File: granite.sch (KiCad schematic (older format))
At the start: 15 parts, among them IC1 ATMEGA32U4, SW1 SW_PUSH, Y1 16MHz

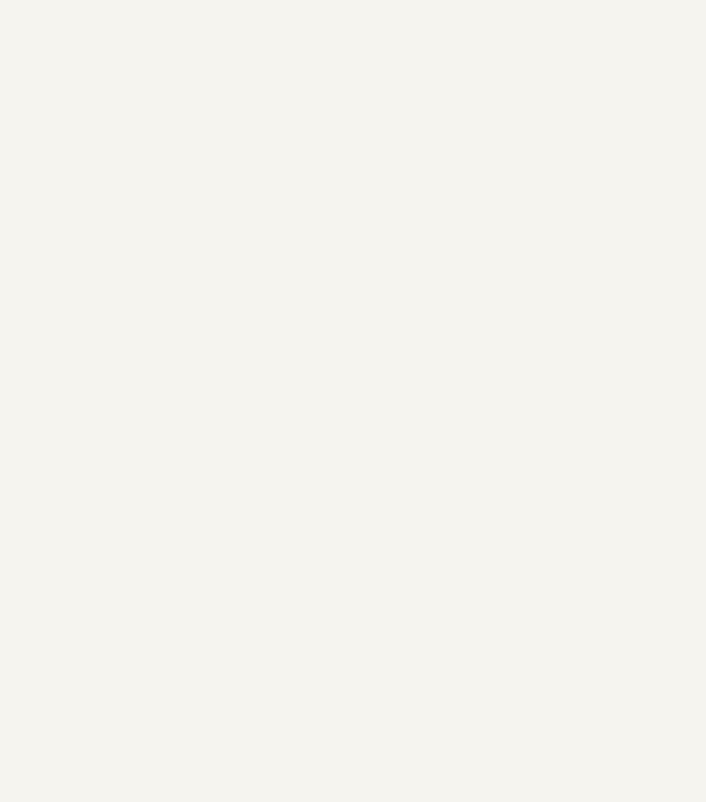
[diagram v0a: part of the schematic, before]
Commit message: usb footprint
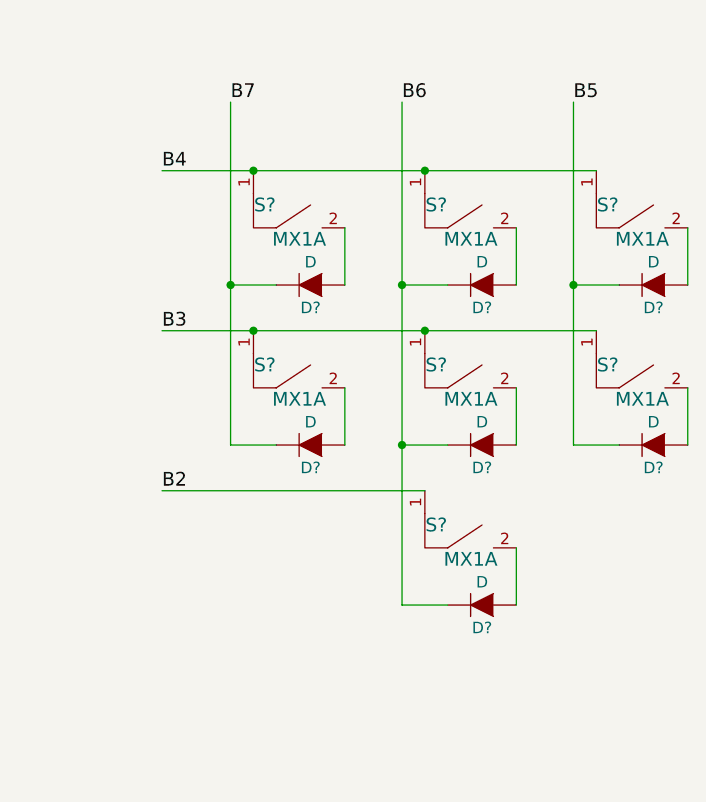
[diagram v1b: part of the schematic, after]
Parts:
- added D? (x7): D, symbol D
- added S? (x7): MX1A, symbol MX1A
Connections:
- net B2: now also S?.1
- net B3: now also S?.1, S?.1, S?.1
- net B4: now also S?.1, S?.1, S?.1
- net B5: now also D?.2 (K), D?.2 (K)
- net B6: now also D?.2 (K), D?.2 (K), D?.2 (K)
- net B7: now also D?.2 (K), D?.2 (K)
- new net: D?.1 (A), S?.2 (x7)
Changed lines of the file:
@@
 LIBS:atmega
 LIBS:mx1a
-LIBS:usb-b
 LIBS:granite-cache
 EELAYER 25 0
@@
 	-1   0    0    1
 $EndComp
+$Comp
+L MX1A S?
+U 1 1 55BD7CBD
+P 11700 4200
+F 0 "S?" H 11550 4450 60  0000 C CNN
+F 1 "MX1A" H 11700 4300 60  0000 C CNN
+F 2 "" H 11700 4200 60  0000 C CNN
+F 3 "" H 11700 4200 60  0000 C CNN
+	1    11700 4200
+	1    0    0    -1
+$EndComp
+$Comp
+L D D?
+U 1 1 55BD8384
+P 11750 4300
+F 0 "D?" H 11750 4400 50  0000 C CNN
+F 1 "D" H 11750 4200 50  0000 C CNN
+F 2 "" H 11750 4300 60  0000 C CNN
+F 3 "" H 11750 4300 60  0000 C CNN
+	1    11750 4300
+	-1   0    0    1
+$EndComp
+Wire Wire Line
+	11900 4050 11900 4300
+Wire Wire Line
+	11600 4300 11400 4300
+$Comp
+L MX1A S?
+U 1 1 55BD8711
+P 12450 4200
+F 0 "S?" H 12300 4450 60  0000 C CNN
+F 1 "MX1A" H 12450 4300 60  0000 C CNN
+F 2 "" H 12450 4200 60  0000 C CNN
+F 3 "" H 12450 4200 60  0000 C CNN
+	1    12450 4200
+	1    0    0    -1
+$EndComp
+$Comp
+L D D?
+U 1 1 55BD8717
+P 12500 4300
+F 0 "D?" H 12500 4400 50  0000 C CNN
+F 1 "D" H 12500 4200 50  0000 C CNN
+F 2 "" H 12500 4300 60  0000 C CNN
+F 3 "" H 12500 4300 60  0000 C CNN
+	1    12500 4300
+	-1   0    0    1
+$EndComp
+Wire Wire Line
+	12650 4050 12650 4300
+Wire Wire Line
+	12350 4300 12150 4300
+$Comp
+L MX1A S?
+U 1 1 55BD8B24
+P 13200 4200
+F 0 "S?" H 13050 4450 60  0000 C CNN
+F 1 "MX1A" H 13200 4300 60  0000 C CNN
+F 2 "" H 13200 4200 60  0000 C CNN
+F 3 "" H 13200 4200 60  0000 C CNN
+	1    13200 4200
+	1    0    0    -1
+$EndComp
+$Comp
+L D D?
+U 1 1 55BD8B2A
+P 13250 4300
+F 0 "D?" H 13250 4400 50  0000 C CNN
+F 1 "D" H 13250 4200 50  0000 C CNN
+F 2 "" H 13250 4300 60  0000 C CNN
+F 3 "" H 13250 4300 60  0000 C CNN
+	1    13250 4300
+	-1   0    0    1
+$EndComp
+Wire Wire Line
+	13400 4050 13400 4300
+Wire Wire Line
+	13100 4300 12900 4300
+$Comp
+L MX1A S?
+U 1 1 55BD8CBB
+P 11700 4900
+F 0 "S?" H 11550 5150 60  0000 C CNN
+F 1 "MX1A" H 11700 5000 60  0000 C CNN
+F 2 "" H 11700 4900 60  0000 C CNN
+F 3 "" H 11700 4900 60  0000 C CNN
+	1    11700 4900
+	1    0    0    -1
+$EndComp
+$Comp
+L D D?
+U 1 1 55BD8CC1
+P 11750 5000
+F 0 "D?" H 11750 5100 50  0000 C CNN
+F 1 "D" H 11750 4900 50  0000 C CNN
+F 2 "" H 11750 5000 60  0000 C CNN
+F 3 "" H 11750 5000 60  0000 C CNN
+	1    11750 5000
+	-1   0    0    1
+$EndComp
+Wire Wire Line
+	11900 4750 11900 5000
+Wire Wire Line
+	11600 5000 11400 5000
+$Comp
+L MX1A S?
+U 1 1 55BD8CC9
+P 12450 4900
+F 0 "S?" H 12300 5150 60  0000 C CNN
+F 1 "MX1A" H 12450 5000 60  0000 C CNN
+F 2 "" H 12450 4900 60  0000 C CNN
+F 3 "" H 12450 4900 60  0000 C CNN
+	1    12450 4900
+	1    0    0    -1
+$EndComp
+$Comp
+L D D?
+U 1 1 55BD8CCF
+P 12500 5000
+F 0 "D?" H 12500 5100 50  0000 C CNN
+F 1 "D" H 12500 4900 50  0000 C CNN
+F 2 "" H 12500 5000 60  0000 C CNN
+F 3 "" H 12500 5000 60  0000 C CNN
+	1    12500 5000
+	-1   0    0    1
+$EndComp
+Wire Wire Line
+	12650 4750 12650 5000
+Wire Wire Line
+	12350 5000 12150 5000
+$Comp
+L MX1A S?
+U 1 1 55BD8CD7
+P 13200 4900
+F 0 "S?" H 13050 5150 60  0000 C CNN
+F 1 "MX1A" H 13200 5000 60  0000 C CNN
+F 2 "" H 13200 4900 60  0000 C CNN
+F 3 "" H 13200 4900 60  0000 C CNN
+	1    13200 4900
+	1    0    0    -1
+$EndComp
+$Comp
+L D D?
+U 1 1 55BD8CDD
+P 13250 5000
+F 0 "D?" H 13250 5100 50  0000 C CNN
+F 1 "D" H 13250 4900 50  0000 C CNN
+F 2 "" H 13250 5000 60  0000 C CNN
+F 3 "" H 13250 5000 60  0000 C CNN
+	1    13250 5000
+	-1   0    0    1
+$EndComp
+Wire Wire Line
+	13400 4750 13400 5000
+Wire Wire Line
+	13100 5000 12900 5000
+$Comp
+L MX1A S?
+U 1 1 55BD8D79
+P 12450 5600
+F 0 "S?" H 12300 5850 60  0000 C CNN
+F 1 "MX1A" H 12450 5700 60  0000 C CNN
+F 2 "" H 12450 5600 60  0000 C CNN
+F 3 "" H 12450 5600 60  0000 C CNN
+	1    12450 5600
+	1    0    0    -1
+$EndComp
+$Comp
+L D D?
+U 1 1 55BD8D7F
+P 12500 5700
+F 0 "D?" H 12500 5800 50  0000 C CNN
+F 1 "D" H 12500 5600 50  0000 C CNN
+F 2 "" H 12500 5700 60  0000 C CNN
+F 3 "" H 12500 5700 60  0000 C CNN
+	1    12500 5700
+	-1   0    0    1
+$EndComp
+Wire Wire Line
+	12650 5450 12650 5700
+Wire Wire Line
+	12350 5700 12150 5700
+Wire Wire Line
+	11100 3800 13000 3800
+Connection ~ 12250 3800
+Connection ~ 11500 3800
+Wire Wire Line
+	11100 4500 13000 4500
+Connection ~ 12250 4500
+Connection ~ 11500 4500
+Wire Wire Line
+	11100 5200 12250 5200
+Wire Wire Line
+	11400 5000 11400 3500
+Connection ~ 11400 4300
+Wire Wire Line
+	12150 5700 12150 3500
+Connection ~ 12150 5000
+Connection ~ 12150 4300
+Wire Wire Line
+	12900 5000 12900 3500
+Connection ~ 12900 4300
+Text Label 11400 3500 0    60   ~ 0
+B7
+Text Label 12150 3500 0    60   ~ 0
+B6
+Text Label 12900 3500 0    60   ~ 0
+B5
+Text Label 11100 3800 0    60   ~ 0
+B4
+Text Label 11100 4500 0    60   ~ 0
+B3
+Text Label 11100 5200 0    60   ~ 0
+B2
 $EndSCHEMATC

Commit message: annotations in schematic
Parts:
- gave numbers to parts that had none: 15
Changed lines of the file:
@@
 F0
 $Comp
-L USB-MINI-B CON?
+L USB-MINI-B CON1
 U 1 1 55B72E69
 P 1850 6250
-F 0 "CON?" H 2100 6600 50  0000 C CNN
+F 0 "CON1" H 2100 6600 50  0000 C CNN
 F 1 "USB-MINI-B WM17115-ND" H 2000 5900 50  0000 C CNN
 F 2 "" H 1850 6150 50  0000 C CNN
@@
 	1100 6200 1100 6350
 $Comp
-L GNDREF #PWR?
+L GNDREF #PWR010
 U 1 1 55B87288
 P 1100 6350
-F 0 "#PWR?" H 1100 6100 60  0001 C CNN
+F 0 "#PWR010" H 1100 6100 60  0001 C CNN
 F 1 "GNDREF" H 1100 6200 60  0000 C CNN
 F 2 "" H 1100 6350 60  0000 C CNN
@@
 	3050 7000 3050 7450
 $Comp
-L GNDREF #PWR?
+L GNDREF #PWR011
 U 1 1 55B88521
 P 3050 7450
-F 0 "#PWR?" H 3050 7200 60  0001 C CNN
+F 0 "#PWR011" H 3050 7200 60  0001 C CNN
 F 1 "GNDREF" H 3050 7300 60  0000 C CNN
 F 2 "" H 3050 7450 60  0000 C CNN
@@
 	1100 5500 3450 5500
 $Comp
-L GNDREF #PWR?
+L GNDREF #PWR012
 U 1 1 55BC6395
 P 1600 6650
-F 0 "#PWR?" H 1600 6400 60  0001 C CNN
+F 0 "#PWR012" H 1600 6400 60  0001 C CNN
 F 1 "GNDREF" H 1600 6500 60  0000 C CNN
 F 2 "" H 1600 6650 60  0000 C CNN
@@
 $EndComp
 $Comp
-L GNDREF #PWR?
+L GNDREF #PWR013
 U 1 1 55BC6520
 P 1600 5850
-F 0 "#PWR?" H 1600 5600 60  0001 C CNN
+F 0 "#PWR013" H 1600 5600 60  0001 C CNN
 F 1 "GNDREF" H 1600 5700 60  0000 C CNN
 F 2 "" H 1600 5850 60  0000 C CNN
@@
 $EndComp
 $Comp
-L MX1A S?
+L MX1A S1
 U 1 1 55BD7CBD
 P 11700 4200
-F 0 "S?" H 11550 4450 60  0000 C CNN
+F 0 "S1" H 11550 4450 60  0000 C CNN
 F 1 "MX1A" H 11700 4300 60  0000 C CNN
 F 2 "" H 11700 4200 60  0000 C CNN
@@
 $EndComp
 $Comp
-L D D?
+L D D1
 U 1 1 55BD8384
 P 11750 4300
-F 0 "D?" H 11750 4400 50  0000 C CNN
+F 0 "D1" H 11750 4400 50  0000 C CNN
 F 1 "D" H 11750 4200 50  0000 C CNN
 F 2 "" H 11750 4300 60  0000 C CNN
@@
 	11600 4300 11400 4300
 $Comp
-L MX1A S?
+L MX1A S3
 U 1 1 55BD8711
 P 12450 4200
-F 0 "S?" H 12300 4450 60  0000 C CNN
+F 0 "S3" H 12300 4450 60  0000 C CNN
 F 1 "MX1A" H 12450 4300 60  0000 C CNN
 F 2 "" H 12450 4200 60  0000 C CNN
@@
 $EndComp
 $Comp
-L D D?
+L D D3
 U 1 1 55BD8717
 P 12500 4300
-F 0 "D?" H 12500 4400 50  0000 C CNN
+F 0 "D3" H 12500 4400 50  0000 C CNN
 F 1 "D" H 12500 4200 50  0000 C CNN
 F 2 "" H 12500 4300 60  0000 C CNN
@@
 	12350 4300 12150 4300
 $Comp
-L MX1A S?
+L MX1A S6
 U 1 1 55BD8B24
 P 13200 4200
-F 0 "S?" H 13050 4450 60  0000 C CNN
+F 0 "S6" H 13050 4450 60  0000 C CNN
 F 1 "MX1A" H 13200 4300 60  0000 C CNN
 F 2 "" H 13200 4200 60  0000 C CNN
@@
 $EndComp
 $Comp
-L D D?
+L D D6
 U 1 1 55BD8B2A
 P 13250 4300
-F 0 "D?" H 13250 4400 50  0000 C CNN
+F 0 "D6" H 13250 4400 50  0000 C CNN
 F 1 "D" H 13250 4200 50  0000 C CNN
 F 2 "" H 13250 4300 60  0000 C CNN
@@
 	13100 4300 12900 4300
 $Comp
-L MX1A S?
+L MX1A S2
 U 1 1 55BD8CBB
 P 11700 4900
-F 0 "S?" H 11550 5150 60  0000 C CNN
+F 0 "S2" H 11550 5150 60  0000 C CNN
 F 1 "MX1A" H 11700 5000 60  0000 C CNN
 F 2 "" H 11700 4900 60  0000 C CNN
@@
 $EndComp
 $Comp
-L D D?
+L D D2
 U 1 1 55BD8CC1
 P 11750 5000
-F 0 "D?" H 11750 5100 50  0000 C CNN
+F 0 "D2" H 11750 5100 50  0000 C CNN
 F 1 "D" H 11750 4900 50  0000 C CNN
 F 2 "" H 11750 5000 60  0000 C CNN
@@
 	11600 5000 11400 5000
 $Comp
-L MX1A S?
+L MX1A S4
 U 1 1 55BD8CC9
 P 12450 4900
-F 0 "S?" H 12300 5150 60  0000 C CNN
+F 0 "S4" H 12300 5150 60  0000 C CNN
 F 1 "MX1A" H 12450 5000 60  0000 C CNN
 F 2 "" H 12450 4900 60  0000 C CNN
@@
 $EndComp
 $Comp
-L D D?
+L D D4
 U 1 1 55BD8CCF
 P 12500 5000
-F 0 "D?" H 12500 5100 50  0000 C CNN
+F 0 "D4" H 12500 5100 50  0000 C CNN
 F 1 "D" H 12500 4900 50  0000 C CNN
 F 2 "" H 12500 5000 60  0000 C CNN
@@
 	12350 5000 12150 5000
 $Comp
-L MX1A S?
+L MX1A S7
 U 1 1 55BD8CD7
 P 13200 4900
-F 0 "S?" H 13050 5150 60  0000 C CNN
+F 0 "S7" H 13050 5150 60  0000 C CNN
 F 1 "MX1A" H 13200 5000 60  0000 C CNN
 F 2 "" H 13200 4900 60  0000 C CNN
@@
 $EndComp
 $Comp
-L D D?
+L D D7
 U 1 1 55BD8CDD
 P 13250 5000
-F 0 "D?" H 13250 5100 50  0000 C CNN
+F 0 "D7" H 13250 5100 50  0000 C CNN
 F 1 "D" H 13250 4900 50  0000 C CNN
 F 2 "" H 13250 5000 60  0000 C CNN
@@
 	13100 5000 12900 5000
 $Comp
-L MX1A S?
+L MX1A S5
 U 1 1 55BD8D79
 P 12450 5600
-F 0 "S?" H 12300 5850 60  0000 C CNN
+F 0 "S5" H 12300 5850 60  0000 C CNN
 F 1 "MX1A" H 12450 5700 60  0000 C CNN
 F 2 "" H 12450 5600 60  0000 C CNN
@@
 $EndComp
 $Comp
-L D D?
+L D D5
 U 1 1 55BD8D7F
 P 12500 5700
-F 0 "D?" H 12500 5800 50  0000 C CNN
+F 0 "D5" H 12500 5800 50  0000 C CNN
 F 1 "D" H 12500 5600 50  0000 C CNN
 F 2 "" H 12500 5700 60  0000 C CNN

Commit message: mx1a footprints
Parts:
- C1, C2, C3: value 0.1uF -> 100nF; footprint Capacitors_SMD:C_0603_HandSoldering -> Capacitors_SMD:C_0805_HandSoldering
- C4, C5, C6: footprint Capacitors_SMD:C_0603_HandSoldering -> Capacitors_SMD:C_0805_HandSoldering
- C7: value 0.1uF -> 100nF; footprint (none) -> Capacitors_SMD:C_0805_HandSoldering
- C8: footprint (none) -> Capacitors_SMD:C_0805_HandSoldering
- CON1: footprint (none) -> bwu-keyboard:USB-MINI-B-WM17115-ND
- D0:0: renamed from D1; footprint (none) -> SM0805:SOD-123
- D0:1: renamed from D3; footprint (none) -> SM0805:SOD-123
- D0:2: renamed from D6; footprint (none) -> SM0805:SOD-123
- D1:0: renamed from D2; footprint (none) -> SM0805:SOD-123
- D1:1: renamed from D4; footprint (none) -> SM0805:SOD-123
- D1:2: renamed from D7; footprint (none) -> SM0805:SOD-123
- D2:1: renamed from D5; footprint (none) -> SM0805:SOD-123
- R1, R2, R3: footprint Resistors_SMD:R_0603_HandSoldering -> Resistors_SMD:R_0805_HandSoldering
- S0:0: renamed from S1; footprint (none) -> CHERRY_PCB_100H:CHERRY_PCB_100H
- S0:1: renamed from S3; footprint (none) -> CHERRY_PCB_100H:CHERRY_PCB_100H
- S0:2: renamed from S6; footprint (none) -> CHERRY_PCB_100H:CHERRY_PCB_100H
- S1:0: renamed from S2; footprint (none) -> CHERRY_PCB_100H:CHERRY_PCB_100H
- S1:1: renamed from S4; footprint (none) -> CHERRY_PCB_100H:CHERRY_PCB_100H
- S1:2: renamed from S7; footprint (none) -> CHERRY_PCB_100H:CHERRY_PCB_100H
- S2:1: renamed from S5; footprint (none) -> CHERRY_PCB_100H:CHERRY_PCB_100H
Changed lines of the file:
@@
 LIBS:atmega
 LIBS:mx1a
+LIBS:usb-b
 LIBS:granite-cache
 EELAYER 25 0
@@
 F 0 "C6" H 2775 6950 50  0000 L CNN
 F 1 "1uF" H 2775 6750 50  0000 L CNN
-F 2 "Capacitors_SMD:C_0603_HandSoldering" H 2750 6850 60  0001 C CNN
+F 2 "Capacitors_SMD:C_0805_HandSoldering" H 2750 6850 60  0001 C CNN
 F 3 "" H 2750 6850 60  0000 C CNN
 	1    2750 6850
@@
 P 3000 3400
 F 0 "C3" H 3025 3500 50  0000 L CNN
-F 1 "0.1uF" H 3025 3300 50  0000 L CNN
-F 2 "Capacitors_SMD:C_0603_HandSoldering" H 3000 3400 60  0001 C CNN
+F 1 "100nF" H 3025 3300 50  0000 L CNN
+F 2 "Capacitors_SMD:C_0805_HandSoldering" H 3000 3400 60  0001 C CNN
 F 3 "" H 3000 3400 60  0000 C CNN
 	1    3000 3400
@@
 P 2700 3400
 F 0 "C2" H 2725 3500 50  0000 L CNN
-F 1 "0.1uF" H 2725 3300 50  0000 L CNN
-F 2 "Capacitors_SMD:C_0603_HandSoldering" H 2700 3400 60  0001 C CNN
+F 1 "100nF" H 2725 3300 50  0000 L CNN
+F 2 "Capacitors_SMD:C_0805_HandSoldering" H 2700 3400 60  0001 C CNN
 F 3 "" H 2700 3400 60  0000 C CNN
 	1    2700 3400
@@
 P 2400 3400
 F 0 "C1" H 2425 3500 50  0000 L CNN
-F 1 "0.1uF" H 2425 3300 50  0000 L CNN
-F 2 "Capacitors_SMD:C_0603_HandSoldering" H 2400 3400 60  0001 C CNN
+F 1 "100nF" H 2425 3300 50  0000 L CNN
+F 2 "Capacitors_SMD:C_0805_HandSoldering" H 2400 3400 60  0001 C CNN
 F 3 "" H 2400 3400 60  0000 C CNN
 	1    2400 3400
@@
 F 0 "R2" V 3030 6300 50  0000 C CNN
 F 1 "22" V 2950 6300 50  0000 C CNN
-F 2 "Resistors_SMD:R_0603_HandSoldering" V 2880 6300 30  0001 C CNN
+F 2 "Resistors_SMD:R_0805_HandSoldering" V 2880 6300 30  0001 C CNN
 F 3 "" H 2950 6300 30  0000 C CNN
 	1    2950 6300
@@
 F 0 "R1" V 3030 6100 50  0000 C CNN
 F 1 "22" V 2950 6100 50  0000 C CNN
-F 2 "Resistors_SMD:R_0603_HandSoldering" V 2880 6100 30  0001 C CNN
+F 2 "Resistors_SMD:R_0805_HandSoldering" V 2880 6100 30  0001 C CNN
 F 3 "" H 2950 6100 30  0000 C CNN
 	1    2950 6100
@@
 F 0 "C4" H 2125 5000 50  0000 L CNN
 F 1 "10pF" H 2125 4800 50  0000 L CNN
-F 2 "Capacitors_SMD:C_0603_HandSoldering" H 2100 4900 60  0001 C CNN
+F 2 "Capacitors_SMD:C_0805_HandSoldering" H 2100 4900 60  0001 C CNN
 F 3 "" H 2100 4900 60  0000 C CNN
 	1    2100 4900
@@
 F 0 "C5" H 2725 5000 50  0000 L CNN
 F 1 "10pF" H 2725 4800 50  0000 L CNN
-F 2 "Capacitors_SMD:C_0603_HandSoldering" H 2700 4900 60  0001 C CNN
+F 2 "Capacitors_SMD:C_0805_HandSoldering" H 2700 4900 60  0001 C CNN
 F 3 "" H 2700 4900 60  0000 C CNN
 	1    2700 4900
@@
 F 0 "R3" V 5280 7400 50  0000 C CNN
 F 1 "1K" V 5200 7400 50  0000 C CNN
-F 2 "Resistors_SMD:R_0603_HandSoldering" V 5130 7400 30  0001 C CNN
+F 2 "Resistors_SMD:R_0805_HandSoldering" V 5130 7400 30  0001 C CNN
 F 3 "" H 5200 7400 30  0000 C CNN
 	1    5200 7400
@@
 F 0 "CON1" H 2100 6600 50  0000 C CNN
 F 1 "USB-MINI-B WM17115-ND" H 2000 5900 50  0000 C CNN
-F 2 "" H 1850 6150 50  0000 C CNN
+F 2 "bwu-keyboard:USB-MINI-B-WM17115-ND" H 1850 6150 50  0001 C CNN
 F 3 "" H 1850 6150 50  0000 C CNN
 	1    1850 6250
@@
 P 1100 6050
 F 0 "C7" H 1125 6150 50  0000 L CNN
-F 1 "0.1uF" H 1125 5950 50  0000 L CNN
-F 2 "" H 1100 6050 60  0000 C CNN
+F 1 "100nF" H 1125 5950 50  0000 L CNN
+F 2 "Capacitors_SMD:C_0805_HandSoldering" H 1100 6050 60  0001 C CNN
 F 3 "" H 1100 6050 60  0000 C CNN
 	1    1100 6050
@@
 F 0 "C8" H 3075 6950 50  0000 L CNN
 F 1 "1uF" H 3075 6750 50  0000 L CNN
-F 2 "" H 3050 6850 60  0000 C CNN
+F 2 "Capacitors_SMD:C_0805_HandSoldering" H 3050 6850 60  0001 C CNN
 F 3 "" H 3050 6850 60  0000 C CNN
 	1    3050 6850
@@
 $EndComp
 $Comp
-L MX1A S1
+L MX1A S0:0
 U 1 1 55BD7CBD
 P 11700 4200
-F 0 "S1" H 11550 4450 60  0000 C CNN
+F 0 "S0:0" H 11550 4450 60  0000 C CNN
 F 1 "MX1A" H 11700 4300 60  0000 C CNN
-F 2 "" H 11700 4200 60  0000 C CNN
+F 2 "CHERRY_PCB_100H:CHERRY_PCB_100H" H 11700 4200 60  0001 C CNN
 F 3 "" H 11700 4200 60  0000 C CNN
 	1    11700 4200
@@
 $EndComp
 $Comp
-L D D1
+L D D0:0
 U 1 1 55BD8384
 P 11750 4300
-F 0 "D1" H 11750 4400 50  0000 C CNN
+F 0 "D0:0" H 11750 4400 50  0000 C CNN
 F 1 "D" H 11750 4200 50  0000 C CNN
-F 2 "" H 11750 4300 60  0000 C CNN
+F 2 "SM0805:SOD-123" H 11750 4300 60  0001 C CNN
 F 3 "" H 11750 4300 60  0000 C CNN
 	1    11750 4300
@@
 	11600 4300 11400 4300
 $Comp
-L MX1A S3
+L MX1A S0:1
 U 1 1 55BD8711
 P 12450 4200
-F 0 "S3" H 12300 4450 60  0000 C CNN
+F 0 "S0:1" H 12300 4450 60  0000 C CNN
 F 1 "MX1A" H 12450 4300 60  0000 C CNN
-F 2 "" H 12450 4200 60  0000 C CNN
+F 2 "CHERRY_PCB_100H:CHERRY_PCB_100H" H 12450 4200 60  0001 C CNN
 F 3 "" H 12450 4200 60  0000 C CNN
 	1    12450 4200
@@
 $EndComp
 $Comp
-L D D3
+L D D0:1
 U 1 1 55BD8717
 P 12500 4300
-F 0 "D3" H 12500 4400 50  0000 C CNN
+F 0 "D0:1" H 12500 4400 50  0000 C CNN
 F 1 "D" H 12500 4200 50  0000 C CNN
-F 2 "" H 12500 4300 60  0000 C CNN
+F 2 "SM0805:SOD-123" H 12500 4300 60  0001 C CNN
 F 3 "" H 12500 4300 60  0000 C CNN
 	1    12500 4300
@@
 	12350 4300 12150 4300
 $Comp
-L MX1A S6
+L MX1A S0:2
 U 1 1 55BD8B24
 P 13200 4200
-F 0 "S6" H 13050 4450 60  0000 C CNN
+F 0 "S0:2" H 13050 4450 60  0000 C CNN
 F 1 "MX1A" H 13200 4300 60  0000 C CNN
-F 2 "" H 13200 4200 60  0000 C CNN
+F 2 "CHERRY_PCB_100H:CHERRY_PCB_100H" H 13200 4200 60  0001 C CNN
 F 3 "" H 13200 4200 60  0000 C CNN
 	1    13200 4200
@@
 $EndComp
 $Comp
-L D D6
+L D D0:2
 U 1 1 55BD8B2A
 P 13250 4300
-F 0 "D6" H 13250 4400 50  0000 C CNN
+F 0 "D0:2" H 13250 4400 50  0000 C CNN
 F 1 "D" H 13250 4200 50  0000 C CNN
-F 2 "" H 13250 4300 60  0000 C CNN
+F 2 "SM0805:SOD-123" H 13250 4300 60  0001 C CNN
 F 3 "" H 13250 4300 60  0000 C CNN
 	1    13250 4300
@@
 	13100 4300 12900 4300
 $Comp
-L MX1A S2
+L MX1A S1:0
 U 1 1 55BD8CBB
 P 11700 4900
-F 0 "S2" H 11550 5150 60  0000 C CNN
+F 0 "S1:0" H 11550 5150 60  0000 C CNN
 F 1 "MX1A" H 11700 5000 60  0000 C CNN
-F 2 "" H 11700 4900 60  0000 C CNN
+F 2 "CHERRY_PCB_100H:CHERRY_PCB_100H" H 11700 4900 60  0001 C CNN
 F 3 "" H 11700 4900 60  0000 C CNN
 	1    11700 4900
@@
 $EndComp
 $Comp
-L D D2
+L D D1:0
 U 1 1 55BD8CC1
 P 11750 5000
-F 0 "D2" H 11750 5100 50  0000 C CNN
+F 0 "D1:0" H 11750 5100 50  0000 C CNN
 F 1 "D" H 11750 4900 50  0000 C CNN
-F 2 "" H 11750 5000 60  0000 C CNN
+F 2 "SM0805:SOD-123" H 11750 5000 60  0001 C CNN
 F 3 "" H 11750 5000 60  0000 C CNN
 	1    11750 5000
@@
 	11600 5000 11400 5000
 $Comp
-L MX1A S4
+L MX1A S1:1
 U 1 1 55BD8CC9
 P 12450 4900
-F 0 "S4" H 12300 5150 60  0000 C CNN
+F 0 "S1:1" H 12300 5150 60  0000 C CNN
 F 1 "MX1A" H 12450 5000 60  0000 C CNN
-F 2 "" H 12450 4900 60  0000 C CNN
+F 2 "CHERRY_PCB_100H:CHERRY_PCB_100H" H 12450 4900 60  0001 C CNN
 F 3 "" H 12450 4900 60  0000 C CNN
 	1    12450 4900
@@
 $EndComp
 $Comp
-L D D4
+L D D1:1
 U 1 1 55BD8CCF
 P 12500 5000
-F 0 "D4" H 12500 5100 50  0000 C CNN
+F 0 "D1:1" H 12500 5100 50  0000 C CNN
 F 1 "D" H 12500 4900 50  0000 C CNN
-F 2 "" H 12500 5000 60  0000 C CNN
+F 2 "SM0805:SOD-123" H 12500 5000 60  0001 C CNN
 F 3 "" H 12500 5000 60  0000 C CNN
 	1    12500 5000
@@
 	12350 5000 12150 5000
 $Comp
-L MX1A S7
+L MX1A S1:2
 U 1 1 55BD8CD7
 P 13200 4900
-F 0 "S7" H 13050 5150 60  0000 C CNN
+F 0 "S1:2" H 13050 5150 60  0000 C CNN
 F 1 "MX1A" H 13200 5000 60  0000 C CNN
-F 2 "" H 13200 4900 60  0000 C CNN
+F 2 "CHERRY_PCB_100H:CHERRY_PCB_100H" H 13200 4900 60  0001 C CNN
 F 3 "" H 13200 4900 60  0000 C CNN
 	1    13200 4900
@@
 $EndComp
 $Comp
-L D D7
+L D D1:2
 U 1 1 55BD8CDD
 P 13250 5000
-F 0 "D7" H 13250 5100 50  0000 C CNN
+F 0 "D1:2" H 13250 5100 50  0000 C CNN
 F 1 "D" H 13250 4900 50  0000 C CNN
-F 2 "" H 13250 5000 60  0000 C CNN
+F 2 "SM0805:SOD-123" H 13250 5000 60  0001 C CNN
 F 3 "" H 13250 5000 60  0000 C CNN
 	1    13250 5000
@@
 	13100 5000 12900 5000
 $Comp
-L MX1A S5
+L MX1A S2:1
 U 1 1 55BD8D79
 P 12450 5600
-F 0 "S5" H 12300 5850 60  0000 C CNN
+F 0 "S2:1" H 12300 5850 60  0000 C CNN
 F 1 "MX1A" H 12450 5700 60  0000 C CNN
-F 2 "" H 12450 5600 60  0000 C CNN
+F 2 "CHERRY_PCB_100H:CHERRY_PCB_100H" H 12450 5600 60  0001 C CNN
 F 3 "" H 12450 5600 60  0000 C CNN
 	1    12450 5600
@@
 $EndComp
 $Comp
-L D D5
+L D D2:1
 U 1 1 55BD8D7F
 P 12500 5700
-F 0 "D5" H 12500 5800 50  0000 C CNN
+F 0 "D2:1" H 12500 5800 50  0000 C CNN
 F 1 "D" H 12500 5600 50  0000 C CNN
-F 2 "" H 12500 5700 60  0000 C CNN
+F 2 "SM0805:SOD-123" H 12500 5700 60  0001 C CNN
 F 3 "" H 12500 5700 60  0000 C CNN
 	1    12500 5700
